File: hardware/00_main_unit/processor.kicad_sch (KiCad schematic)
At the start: 29 parts, among them J13 Conn_01x04_Male, SW2 SW_Push, SW3 SW_Push, U1 STM32H743VIT6, Y1 ABM7-25.000MHZ-D2Y-T

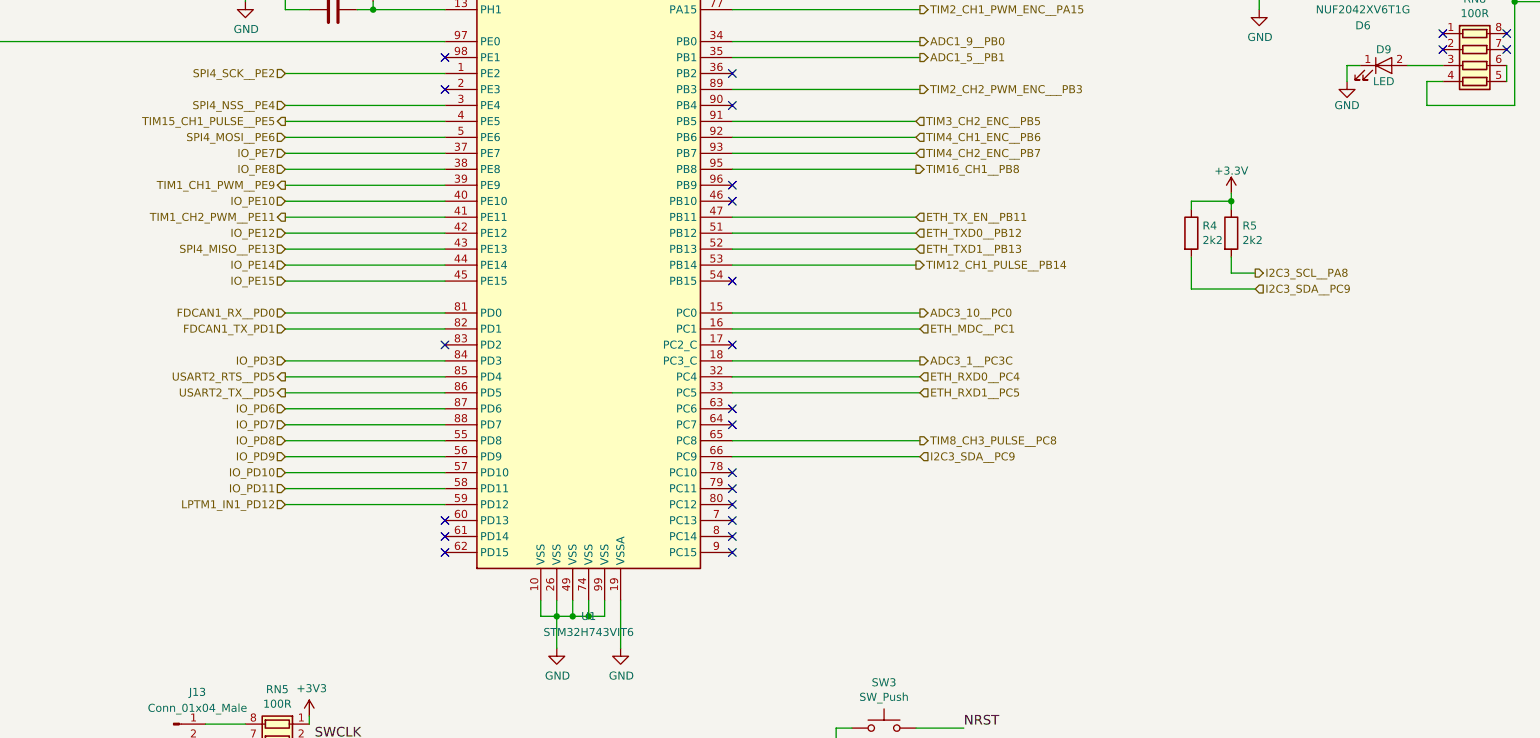
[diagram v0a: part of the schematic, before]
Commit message: Fixes after wrong merge
Signed-off-by: Jacek <matuszewski.kartech@gmail.com>
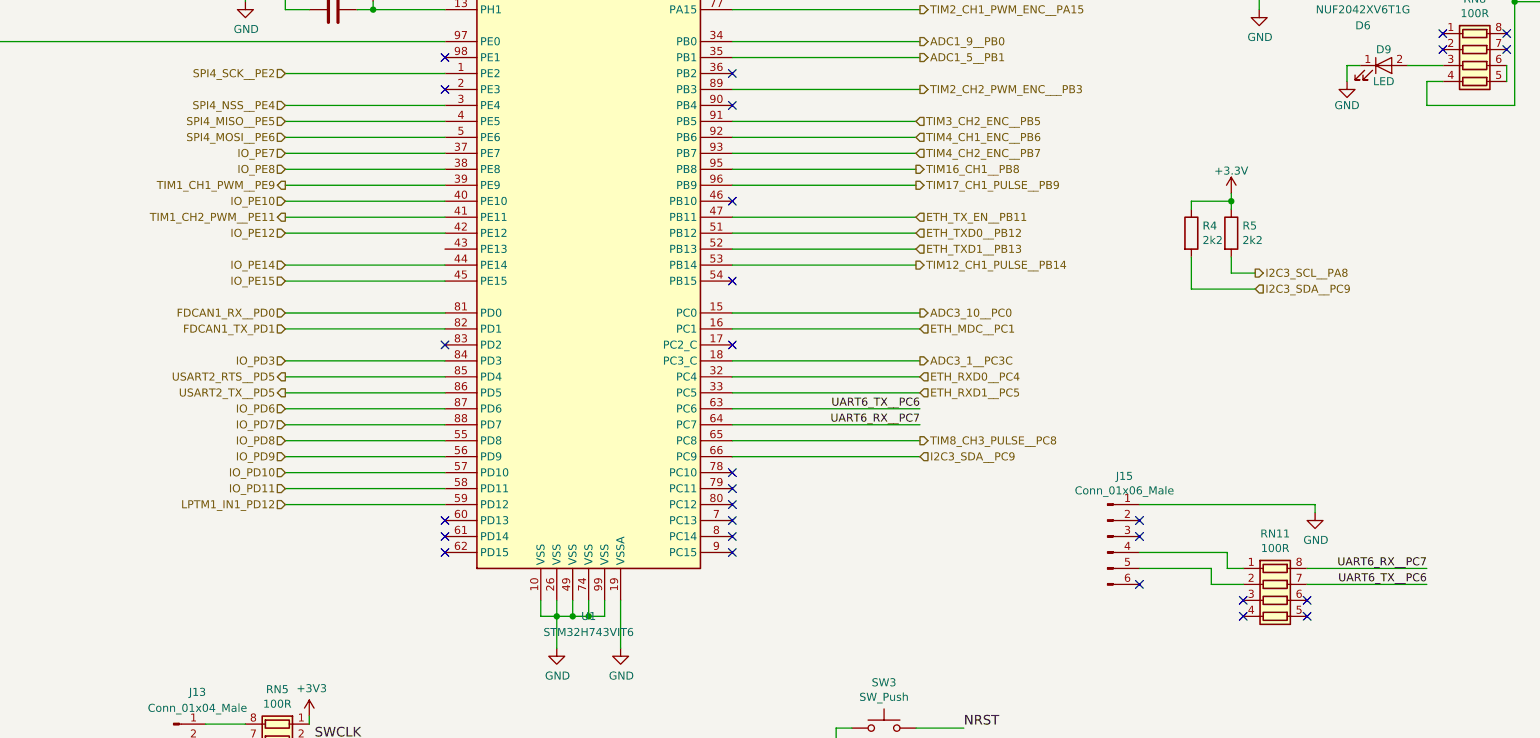
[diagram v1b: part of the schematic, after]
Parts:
- added J15: Conn_01x06_Male, Connector_PinHeader_2.54mm:PinHeader_1x06_P2.54mm_Vertical, symbol Connector:Conn_01x06_Male
- added RN11: 100R, moje:R_Array_Convex_4x0603, symbol Device:R_Pack04
- C10, C11, C13, C23: TME CL10A106MQ8NNNC -> (none)
- C12, C14, C15, C16, C17, C20, C22, C24: TME C0603C104K3RAC -> (none)
- C18, C19: TME 0603N180G500CT -> (none)
- D2, D3, D9: TME LL-S170PGC-G5-1A -> (none)
- R3, R4, R5: TME HP03-2K25% -> (none)
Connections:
- net GND: now also J15.1 (Pin_1)
- net UART6_TX__PC6: now reaches U1.63 (PC6)
- net UART6_TX__PC6: now also RN11.7 (R2.2)
- net UART6_RX__PC7: now reaches U1.64 (PC7)
- net UART6_RX__PC7: now also RN11.8 (R1.2)
- net TIM17_CH1_PULSE__PB9: now reaches U1.96 (PB9)
- net SPI4_MISO__PE13: no longer names the net of U1.43 (PE13)
- net TIM15_CH1_PULSE__PE5 renamed SPI4_MISO__PE5
- new net: J15.4 (Pin_4), RN11.1 (R1.1)
- new net: J15.5 (Pin_5), RN11.2 (R2.1)
- no-connect marks 28 -> 32

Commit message: Fixes before ordering PCB
Signed-off-by: Jarosław Karwik <jaroslaw.karwik@gmail.com>
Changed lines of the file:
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@@
-    (stroke (width 0) (type solid) (color 0 0 0 0))
-  )
-  (wire (pts (xy 172.72 31.75) (xy 179.07 31.75))
     (stroke (width 0) (type solid) (color 0 0 0 0))
   )
@@
     (stroke (width 0) (type solid) (color 0 0 0 0))
   )
+  (wire (pts (xy 179.07 31.75) (xy 172.72 31.75))
+    (stroke (width 0) (type solid) (color 0 0 0 0))
+  )
   (wire (pts (xy 179.07 31.75) (xy 232.41 31.75))
     (stroke (width 0) (type solid) (color 0 0 0 0))
@@
     (stroke (width 0) (type solid) (color 0 0 0 0))
   )
-  (wire (pts (xy 246.38 31.75) (xy 256.54 31.75))
-    (stroke (width 0) (type solid) (color 0 0 0 0))
-  )
   (wire (pts (xy 246.38 38.1) (xy 246.38 31.75))
     (stroke (width 0) (type solid) (color 0 0 0 0))
@@
     (stroke (width 0) (type solid) (color 0 0 0 0))
   )
+  (wire (pts (xy 256.54 31.75) (xy 246.38 31.75))
+    (stroke (width 0) (type solid) (color 0 0 0 0))
+  )

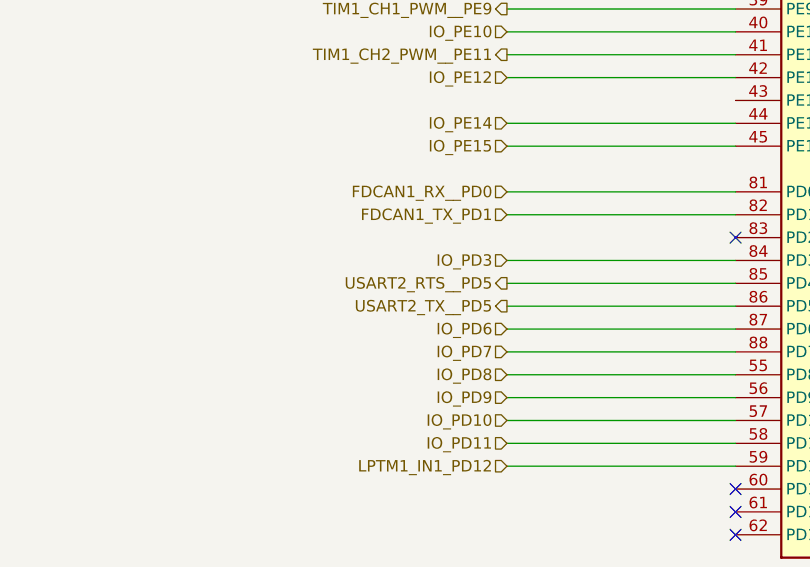
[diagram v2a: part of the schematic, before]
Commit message: Fixes for new hw version
Signed-off-by: Jarosław Karwik <jaroslaw.karwik@gmail.com>
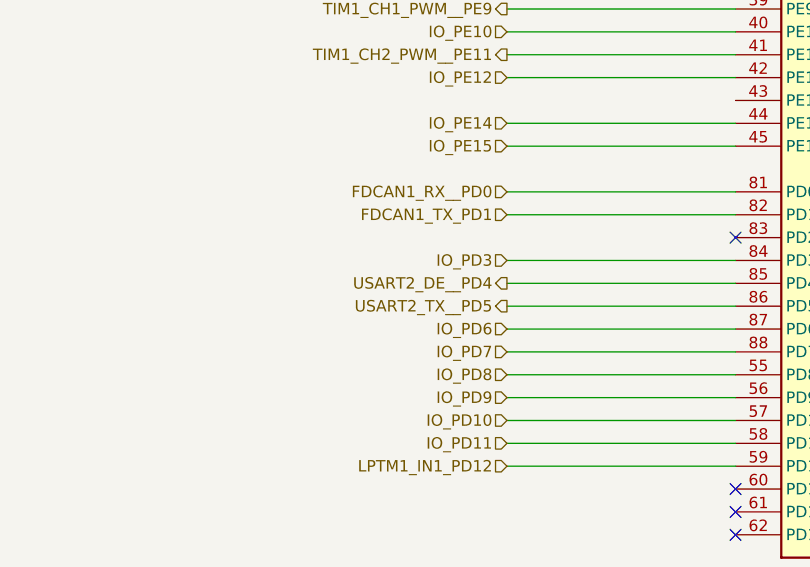
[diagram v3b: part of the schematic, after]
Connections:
- net USART2_RTS__PD5 renamed USART2_DE__PD4
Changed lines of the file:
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@@
     (effects (font (size 1.27 1.27)) (justify right))
   )
-  (hierarchical_label "USART2_RTS__PD5" (shape output) (at 160.02 162.56 180)
+  (hierarchical_label "USART2_DE__PD4" (shape output) (at 160.02 162.56 180)
     (effects (font (size 1.27 1.27)) (justify right))
   )

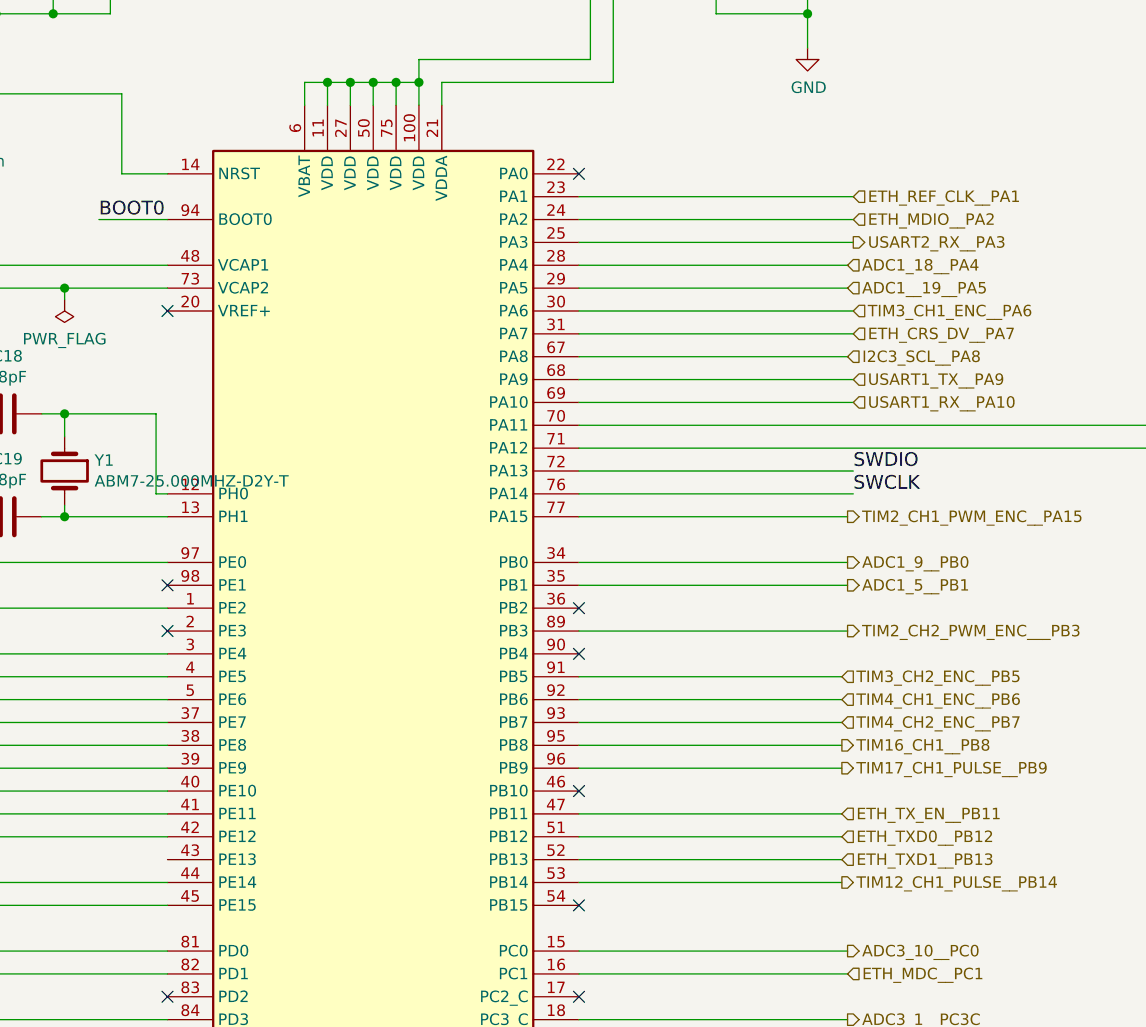
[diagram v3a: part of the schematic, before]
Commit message: Remote mode fixes
Signed-off-by: Jarosław Karwik <jaroslaw.karwik@gmail.com>
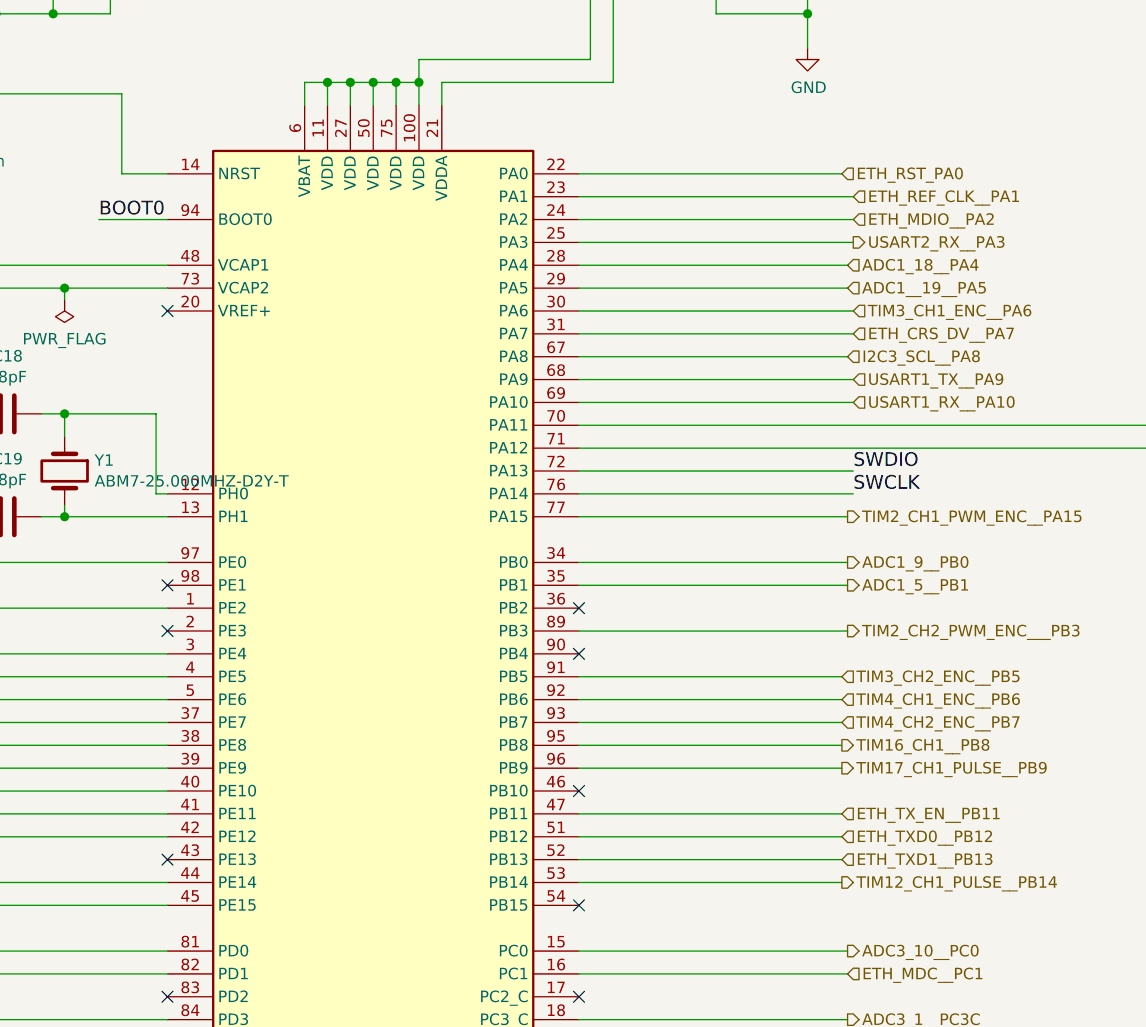
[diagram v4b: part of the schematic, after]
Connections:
- net ETH_RST_PA0: now reaches U1.22 (PA0)

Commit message: FW and SW updates for new revision
Signed-off-by: Jarosław Karwik <jaroslaw.karwik@gmail.com>
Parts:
- removed SW2, SW3: SW_Push, Buttons_Switches_SMD:SW_SPST_B3U-1000P, symbol Uni_Printer-rescue:SW_Push-Switch
- added J9: Conn_02x02_Odd_Even, Connector_PinHeader_2.54mm:PinHeader_2x02_P2.54mm_Vertical, symbol Connector_Generic:Conn_02x02_Odd_Even
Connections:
- net +3V3: now also J9.3 (Pin_3)
- net BOOT0: now also J9.4 (Pin_4)
- net GND: now also J9.1 (Pin_1)
- net NRST: now also J9.2 (Pin_2)
- net IO_PD2: now reaches U1.83 (PD2)
- net FDCAN1_RX__PD0: no longer names the net of U1.81 (PD0)
- net FDCAN1_TX_PD1 renamed IO_PD1
- net LPTM1_IN1_PD12 renamed IO_PD12
- net TIM16_CH1__PB8 renamed IO_PB8
- net USART1_RX__PA10 renamed IO__PA10
- net USART1_TX__PA9 renamed IO__PA9
- net USART2_DE__PD4: no longer names the net of U1.85 (PD4)
- net USART2_RX__PA3: no longer names the net of U1.25 (PA3)
- net USART2_TX__PD5: no longer names the net of U1.86 (PD5)
- no-connect marks 32 -> 35
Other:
- moved on the sheet: R3
